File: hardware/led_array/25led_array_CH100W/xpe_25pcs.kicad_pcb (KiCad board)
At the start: 2 copper layers, 46 x 46 mm, 30 parts, among them J1 Conn_01x10

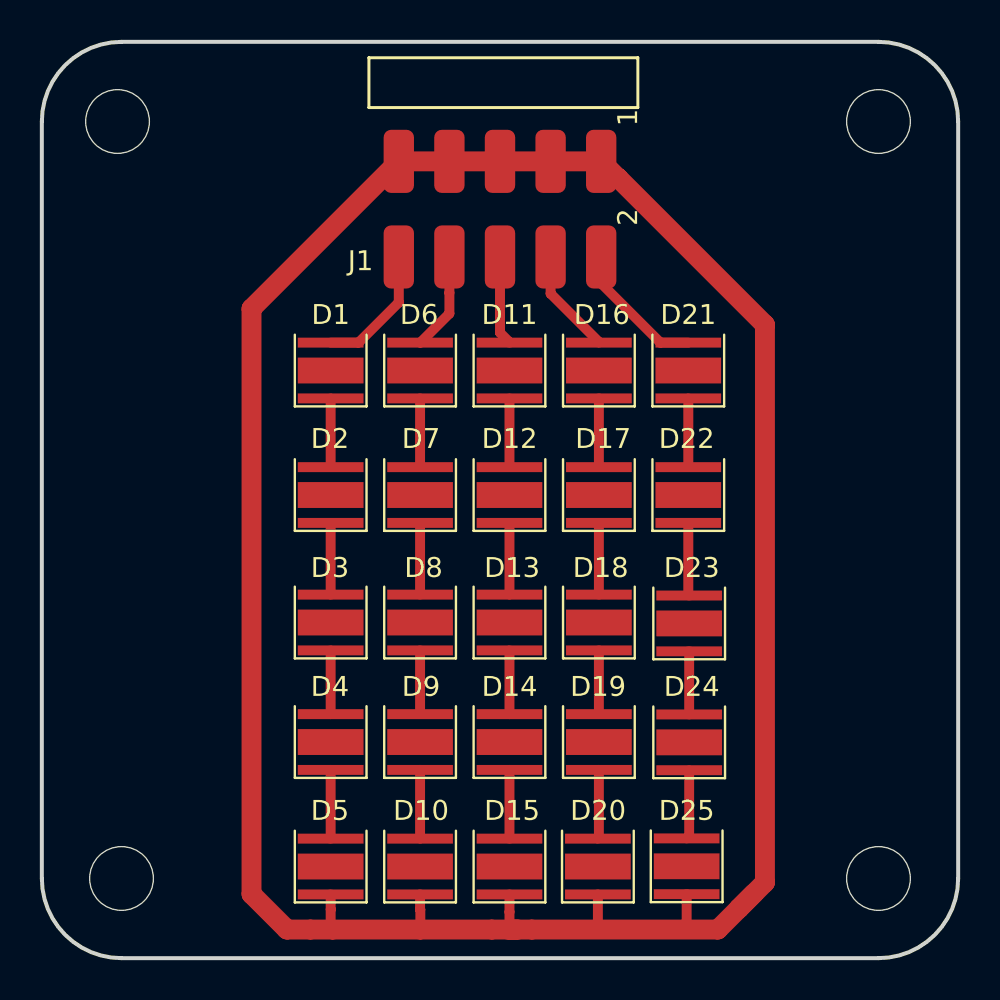
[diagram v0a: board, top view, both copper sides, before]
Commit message: led 25 array rework (fix distance from 38 to 34mm, space between header and led added)
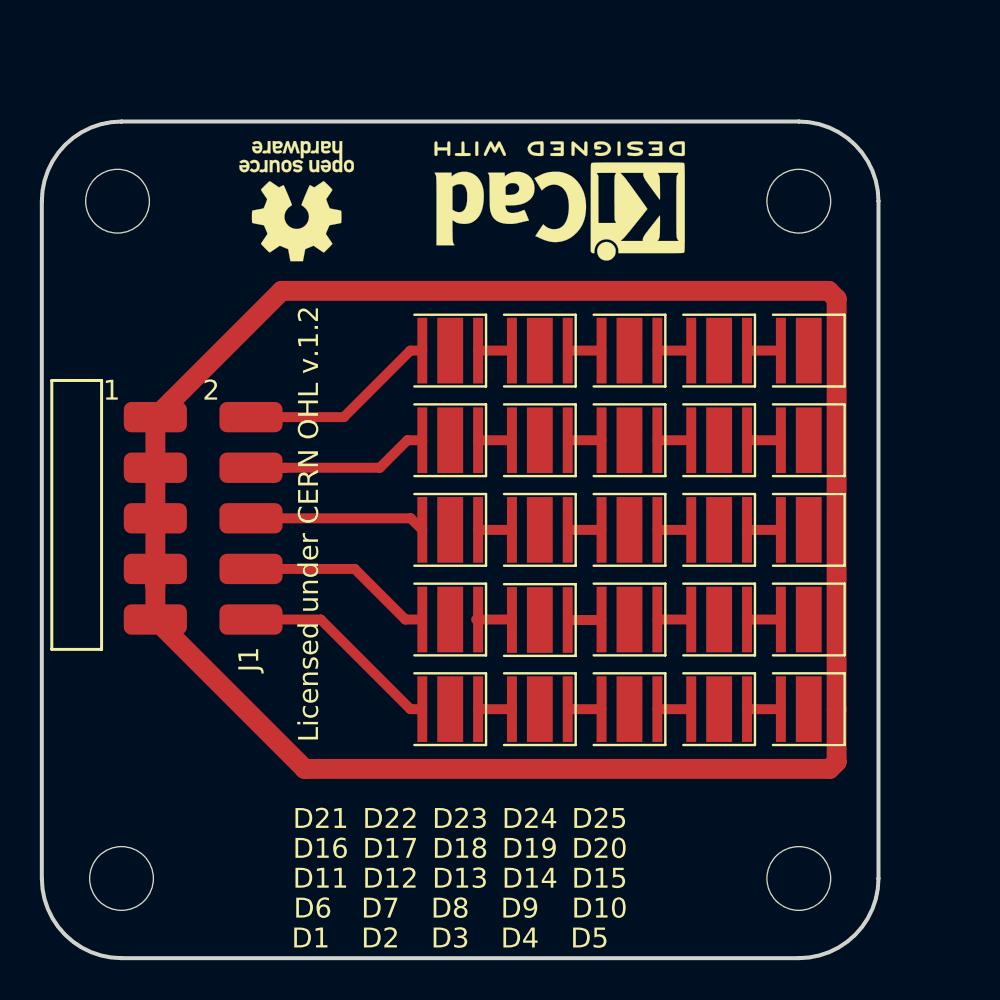
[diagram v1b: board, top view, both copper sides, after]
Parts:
- added REF**: KiCad-Logo2_6mm_SilkScreen, symbol:KiCad-Logo2_6mm_SilkScreen, F.Cu at (89.0, 62.0)
- added REF**: OSHW-Logo_5.7x6mm_SilkScreen, symbol:OSHW-Logo_5.7x6mm_SilkScreen, F.Cu at (75.8, 62.0)
- moved D25 26.6 mm to (101.5, 69.5), turned to 180 degrees
- moved D5 25.3 mm to (101.5, 87.5), turned to 180 degrees
- moved D20 23.9 mm to (101.5, 74.0), turned to 180 degrees
- moved D10 23.1 mm to (101.5, 83.0), turned to 180 degrees
- moved D15 22.6 mm to (101.5, 78.5), turned to 180 degrees
- moved D24 19.7 mm to (97.0, 69.5), turned to 180 degrees
- moved J1 19.7 mm to (73.5, 83.0), turned to 180 degrees
- moved D4 19.6 mm to (97.0, 87.5), turned to 180 degrees
- moved D1 18.0 mm to (83.5, 87.5), turned to 180 degrees
- moved D19 16.3 mm to (97.0, 74.0), turned to 180 degrees
- moved D9 16.2 mm to (97.0, 83.0), turned to 180 degrees
- moved D3 15.6 mm to (92.5, 87.5), turned to 180 degrees
- moved D2 15.0 mm to (88.0, 87.5), turned to 180 degrees
- moved D14 15.0 mm to (97.0, 78.5), turned to 180 degrees
- moved D23 14.0 mm to (92.5, 69.5), turned to 180 degrees
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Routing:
- net GND: track 151.7 -> 107.9 mm
- net Net-(D6-Pad2): track 4.92 -> 9.55 mm
- net Net-(D11-Pad2): track 4.50 -> 8.84 mm
- net Net-(D1-Pad2): track 6.54 -> 10.5 mm
- net Net-(D16-Pad2): track 5.30 -> 9.17 mm
- net Net-(D21-Pad2): track 6.93 -> 9.98 mm
- net Net-(D22-Pad1): track 3.66 -> 1.70 mm
- net Net-(D2-Pad1): track 3.60 -> 1.70 mm
- net Net-(D17-Pad1): track 3.60 -> 1.70 mm
- net Net-(D12-Pad1): track 3.60 -> 1.70 mm
- net Net-(D7-Pad1): track 3.60 -> 1.71 mm
- net Net-(D24-Pad1): track 3.48 -> 1.70 mm
- net Net-(D19-Pad1): track 3.47 -> 1.70 mm
- net Net-(D4-Pad1): track 3.45 -> 1.70 mm
- net Net-(D14-Pad1): track 3.45 -> 1.70 mm
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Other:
- board size 46 x 46 mm -> 42 x 42 mm
- board text added: "Licensed under CERN OHL v.1.2"

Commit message: controller schematic draft finished
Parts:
- added C1: 0.1u, Capacitor_SMD:C_0603_1608Metric_Pad1.05x0.95mm_HandSolder, F.Cu at (95.1, 96.5)
- added TH1: Thermistor, Capacitor_SMD:C_0603_1608Metric_Pad1.05x0.95mm_HandSolder, F.Cu at (95.1, 93.3)
- J1: value Conn_01x10 -> Conn_01x12_Male; footprint led:header_10_smd -> led:header_12_smd
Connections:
- D10 pad 1: GND -> Net-(D10-Pad1)
- D15 pad 1: GND -> Net-(D15-Pad1)
- D20 pad 1: GND -> Net-(D20-Pad1)
- D25 pad 1: GND -> Net-(D25-Pad1)
- D5 pad 1: GND -> Net-(D5-Pad1)
- J1 pad 1: GND -> Net-(D21-Pad2)
- J1 pad 10: Net-(D1-Pad2) -> Net-(D5-Pad1)
- J1 pad 2: Net-(D21-Pad2) -> Net-(D25-Pad1)
- J1 pad 3: GND -> Net-(D16-Pad2)
- J1 pad 4: Net-(D16-Pad2) -> Net-(D20-Pad1)
- J1 pad 5: GND -> Net-(D11-Pad2)
- J1 pad 6: Net-(D11-Pad2) -> Net-(D15-Pad1)
- J1 pad 7: GND -> Net-(D6-Pad2)
- J1 pad 8: Net-(D6-Pad2) -> Net-(D10-Pad1)
- J1 pad 9: GND -> Net-(D1-Pad2)
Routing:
- net GND: track 107.9 -> 0.00 mm
- net Net-(C1-Pad2): track 0.00 -> 37.5 mm
- net Net-(D5-Pad1): track 0.00 -> 34.0 mm
- net Net-(D10-Pad1): track 0.00 -> 33.7 mm
- net Net-(D15-Pad1): track 0.00 -> 32.4 mm
- net Net-(D25-Pad1): track 0.00 -> 31.8 mm
- net Net-(D20-Pad1): track 0.00 -> 31.6 mm
- net Net-(C1-Pad1): track 0.00 -> 28.5 mm
- net Net-(D6-Pad2): track 9.55 -> 15.5 mm
- net Net-(D11-Pad2): track 8.84 -> 14.6 mm
- net Net-(D1-Pad2): track 10.5 -> 16.3 mm
- net Net-(D16-Pad2): track 9.17 -> 14.0 mm
- net Net-(D21-Pad2): track 9.98 -> 14.8 mm

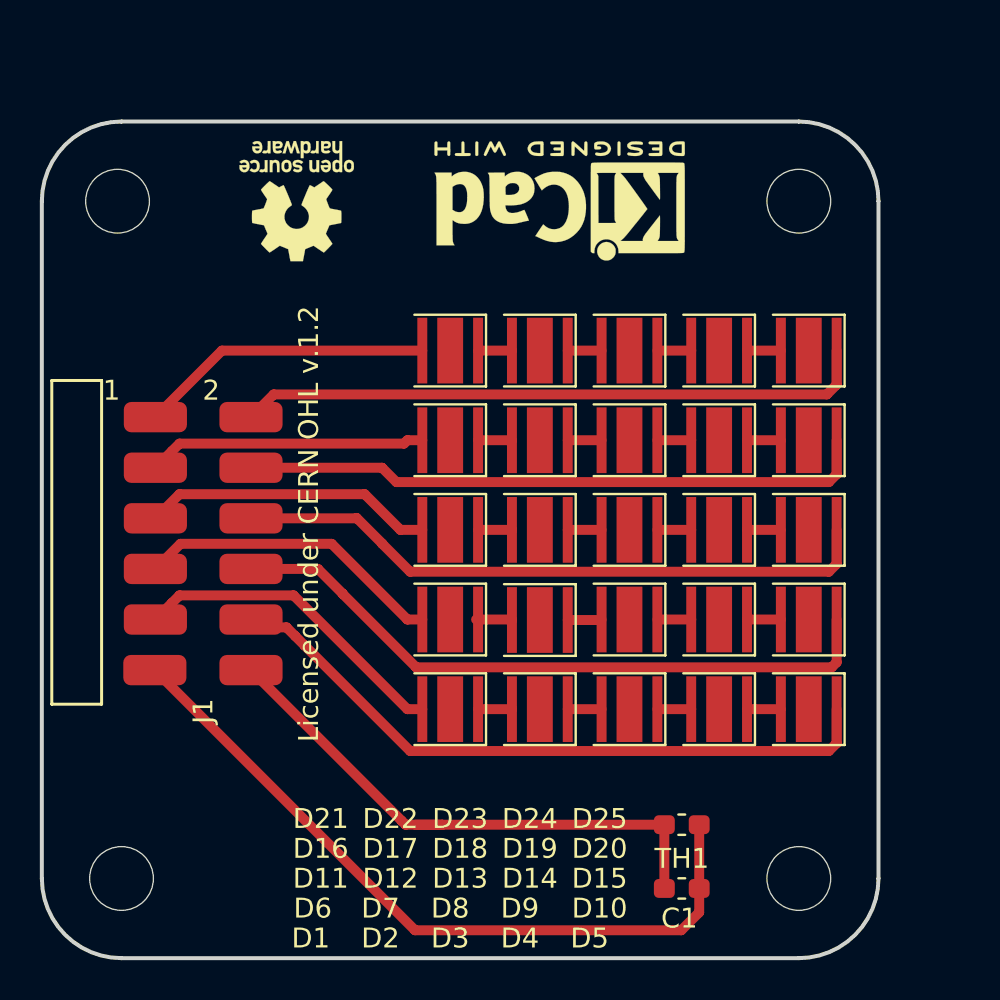
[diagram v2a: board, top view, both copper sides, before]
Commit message: led array rework for fr4 board
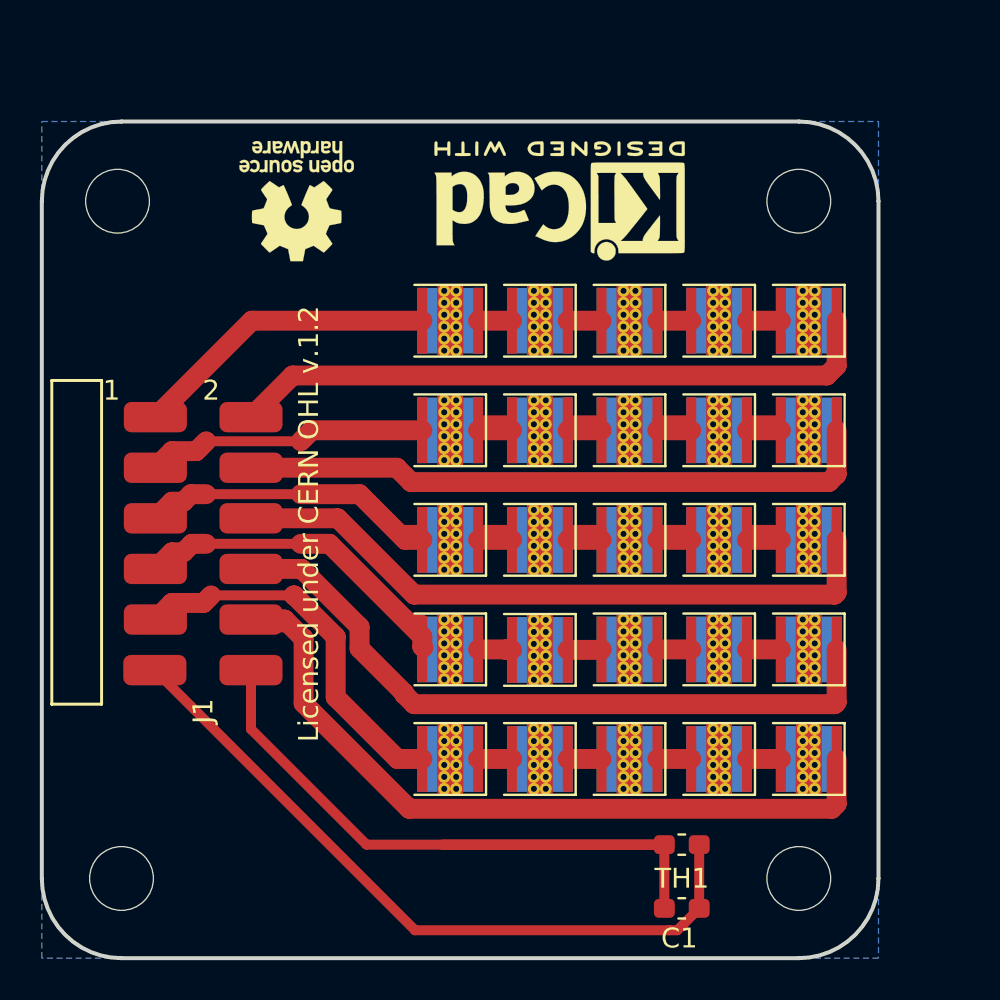
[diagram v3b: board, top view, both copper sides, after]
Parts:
- D1, D10, D11, D12, D13, D14, D15, D16, D17, D18, D19, D2, D20, D21, D22, D23, D24, D25, D3, D4, D5, D6, D7, D8, D9: footprint led:LED_Cree-XP-E -> led:LED_Cree-XP-E_vias
- TH1: value Thermistor -> NTCS0603E3103
- moved D1 2.50 mm to (83.5, 90.0)
- moved D2 2.50 mm to (88.0, 90.0)
- moved D3 2.50 mm to (92.5, 90.0)
- moved D4 2.50 mm to (97.0, 90.0)
- moved D5 2.50 mm to (101.5, 90.0)
- moved D10 1.50 mm to (101.5, 84.5)
- moved D21 1.50 mm to (83.5, 68.0)
- moved D22 1.50 mm to (88.0, 68.0)
- moved D23 1.50 mm to (92.5, 68.0)
- moved D24 1.50 mm to (97.0, 68.0)
- moved D25 1.50 mm to (101.5, 68.0)
- moved D6 1.50 mm to (83.5, 84.5)
- moved D7 1.50 mm to (88.0, 84.5)
- moved D8 1.50 mm to (92.5, 84.5)
- moved D9 1.50 mm to (97.0, 84.5)
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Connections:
- D1 pad 3: (no net) -> p
- D10 pad 3: (no net) -> p
- D11 pad 3: (no net) -> p
- D12 pad 3: (no net) -> p
- D13 pad 3: (no net) -> p
- D14 pad 3: (no net) -> p
- D15 pad 3: (no net) -> p
- D16 pad 3: (no net) -> p
- D17 pad 3: (no net) -> p
- D18 pad 3: (no net) -> p
- D19 pad 3: (no net) -> p
- D2 pad 3: (no net) -> p
- D20 pad 3: (no net) -> p
- D21 pad 3: (no net) -> p
- D22 pad 3: (no net) -> p
- D23 pad 3: (no net) -> p
- D24 pad 3: (no net) -> p
- D25 pad 3: (no net) -> p
- D3 pad 3: (no net) -> p
- D4 pad 3: (no net) -> p
- D5 pad 3: (no net) -> p
- D6 pad 3: (no net) -> p
- D7 pad 3: (no net) -> p
- D8 pad 3: (no net) -> p
- D9 pad 3: (no net) -> p
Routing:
- net Net-(C1-Pad1): track 28.5 -> 54.9 mm
- net Net-(D6-Pad2): track 15.5 -> 24.1 mm
- net Net-(D11-Pad2): track 14.6 -> 21.7 mm
- net Net-(D5-Pad1): track 34.0 -> 40.2 mm
- net Net-(D15-Pad1): track 32.4 -> 35.4 mm
- net Net-(D1-Pad2): track 16.3 -> 19.1 mm
- net Net-(D25-Pad1): track 31.8 -> 34.4 mm
- net Net-(D20-Pad1): track 31.6 -> 33.8 mm
- net Net-(D10-Pad1): track 33.7 -> 35.6 mm
- net Net-(D6-Pad1): track 1.81 -> 3.52 mm
- net Net-(D19-Pad1): track 1.70 -> 3.40 mm
- net Net-(D18-Pad1): track 1.70 -> 3.40 mm
- net Net-(D17-Pad1): track 1.70 -> 3.40 mm
- net Net-(D16-Pad1): track 1.70 -> 3.40 mm
- net Net-(D14-Pad1): track 1.70 -> 3.40 mm
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- added copper zone on B.Cu, net p
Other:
- rule via_min_size: 0.4 -> 0.3
